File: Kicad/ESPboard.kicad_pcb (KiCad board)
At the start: 2 copper layers, 50.5 x 47.2 mm, 36 parts, among them J1 Controls, J2 GPIO 3.3V, J3 GPIO 5V, J4 Input Power, Q1 BSS138, Q2 BSS138, Q3 BSS138, Q4 BSS138, SW1 Reset, SW2 SW_SPST, SW3 SW_SPST, SW4 SW_SPST, SW5 SW_SPST, U1 ESP8266-01_ESP-01, U2 AMS1117-5.0, U3 AMS1117-3.3

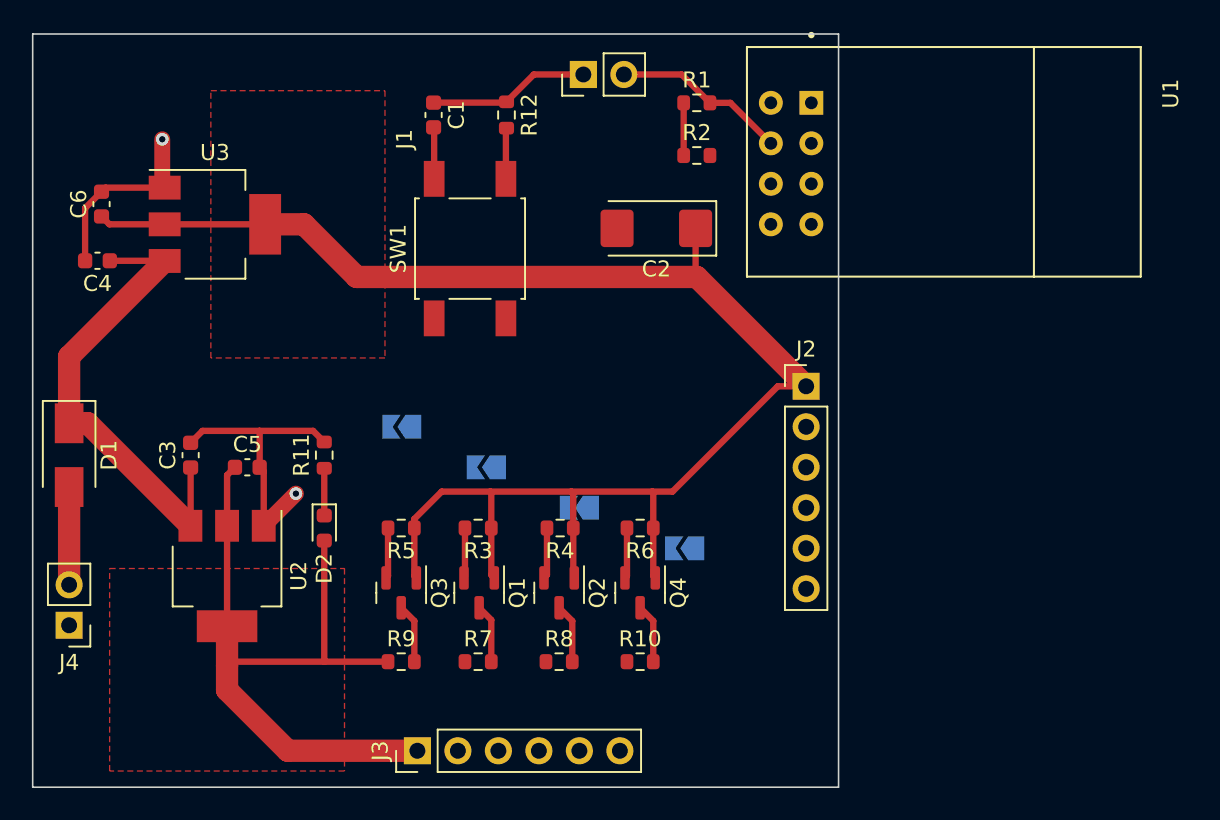
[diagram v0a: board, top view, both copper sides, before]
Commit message: Resized board
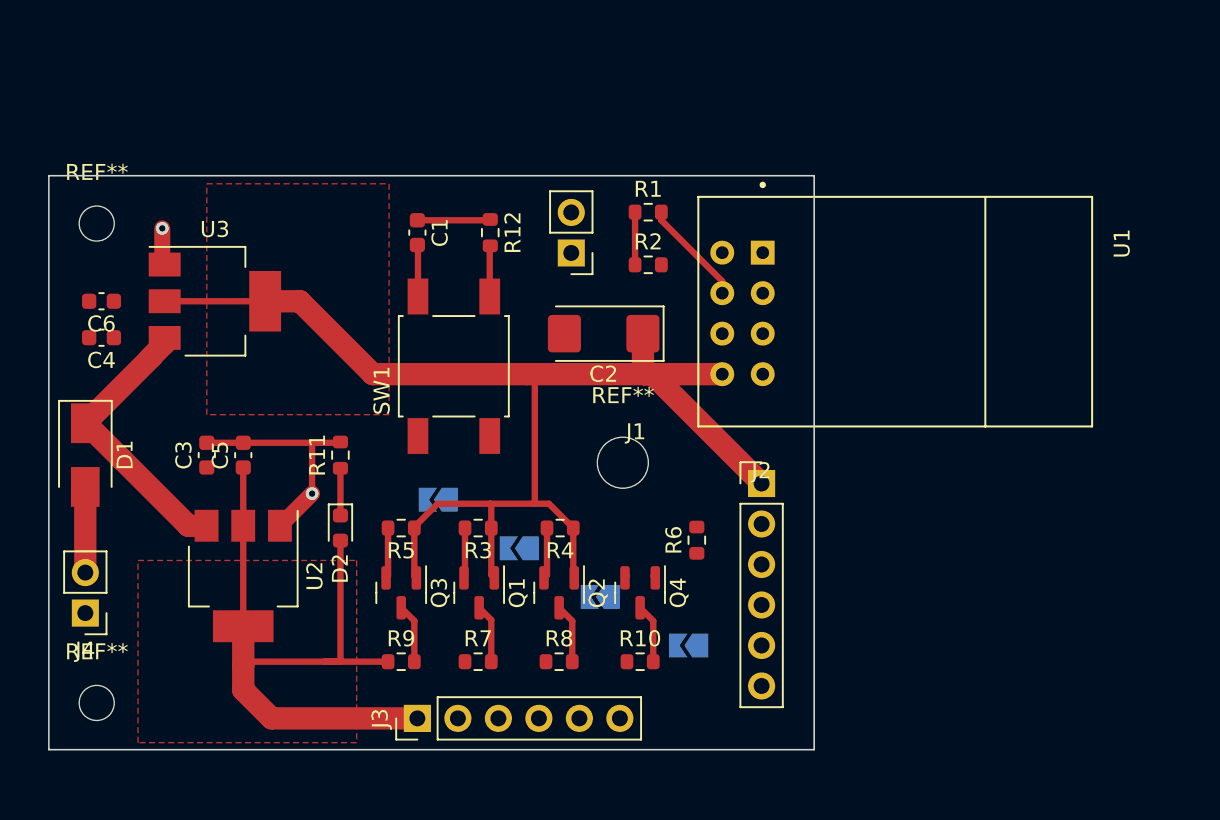
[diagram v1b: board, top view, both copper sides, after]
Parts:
- added REF**: MountingHole_3.2mm_M3, MountingHole:MountingHole_3.2mm_M3, F.Cu at (178.2, 115.5)
- added REF**: MountingHole_2.2mm_M2, MountingHole:MountingHole_2.2mm_M2, F.Cu at (145.2, 100.5)
- added REF**: MountingHole_2.2mm_M2, MountingHole:MountingHole_2.2mm_M2, F.Cu at (145.2, 130.6)
- moved J1 11.2 mm to (175.0, 102.4), turned to 180 degrees
- moved U1 9.88 mm to (195.3, 106.2)
- moved R1 7.50 mm to (179.8, 99.8)
- moved R2 7.50 mm to (179.8, 103.1)
- moved R12 7.45 mm to (169.9, 101.1)
- moved C1 7.45 mm to (165.4, 101.1)
- moved SW1 7.45 mm to (167.6, 109.5)
- moved C2 7.38 mm to (177.0, 107.4)
- moved J2 6.71 mm to (186.9, 116.8)
- moved SW5 6.10 mm to (182.4, 127.0)
- moved C6 6.10 mm to (145.5, 105.4), turned to 180 degrees
- moved SW3 5.74 mm to (176.8, 124.0)
- moved SW2 5.49 mm to (171.7, 120.9)
- moved SW4 5.11 mm to (166.7, 117.9)
- moved C4 4.83 mm to (145.5, 107.7)
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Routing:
- net +3.3V: track 103.3 -> 83.8 mm
- net GND: track 33.1 -> 20.0 mm
- net VCC: track 30.0 -> 17.9 mm
- net Net-(C1-Pad1): track 10.1 -> 4.59 mm
- net Net-(J1-Pad2): track 11.0 -> 6.66 mm
- net Net-(Q4-Pad2): track 3.18 -> 0.18 mm
- net +5V: track 45.5 -> 43.4 mm
- net Net-(D1-Pad2): track 6.13 -> 5.37 mm
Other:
- board size 50.5 x 47.2 mm -> 48 x 36 mm

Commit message: Routing complete
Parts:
- renumbered REF** to H1, REF** to H2, REF** to H3
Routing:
- net Net-(J2-Pad4): track 0.00 -> 35.8 mm
- net Net-(J2-Pad3): track 0.00 -> 33.1 mm
- net Net-(J2-Pad2): track 0.00 -> 31.7 mm
- net Net-(J2-Pad5): track 0.00 -> 24.6 mm
- net Net-(C1-Pad1): track 4.59 -> 28.0 mm
- net GND: track 20.0 -> 43.2 mm, vias 2 -> 3
- net +3.3V: track 83.8 -> 102.0 mm
- net +5V: track 43.4 -> 61.1 mm, vias 0 -> 2
- net Net-(Q4-Pad2): track 0.18 -> 16.1 mm, vias 0 -> 1
- net Net-(J3-Pad4): track 3.72 -> 11.5 mm
- net Net-(J1-Pad2): track 6.66 -> 13.8 mm
- net VCC: track 17.9 -> 24.7 mm
- net Net-(Q2-Pad2): track 3.20 -> 9.68 mm, vias 0 -> 1
- net Net-(Q1-Pad2): track 3.15 -> 9.28 mm, vias 0 -> 1
- net Net-(J3-Pad5): track 3.72 -> 9.83 mm
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- added copper zone on B.Cu, net GND

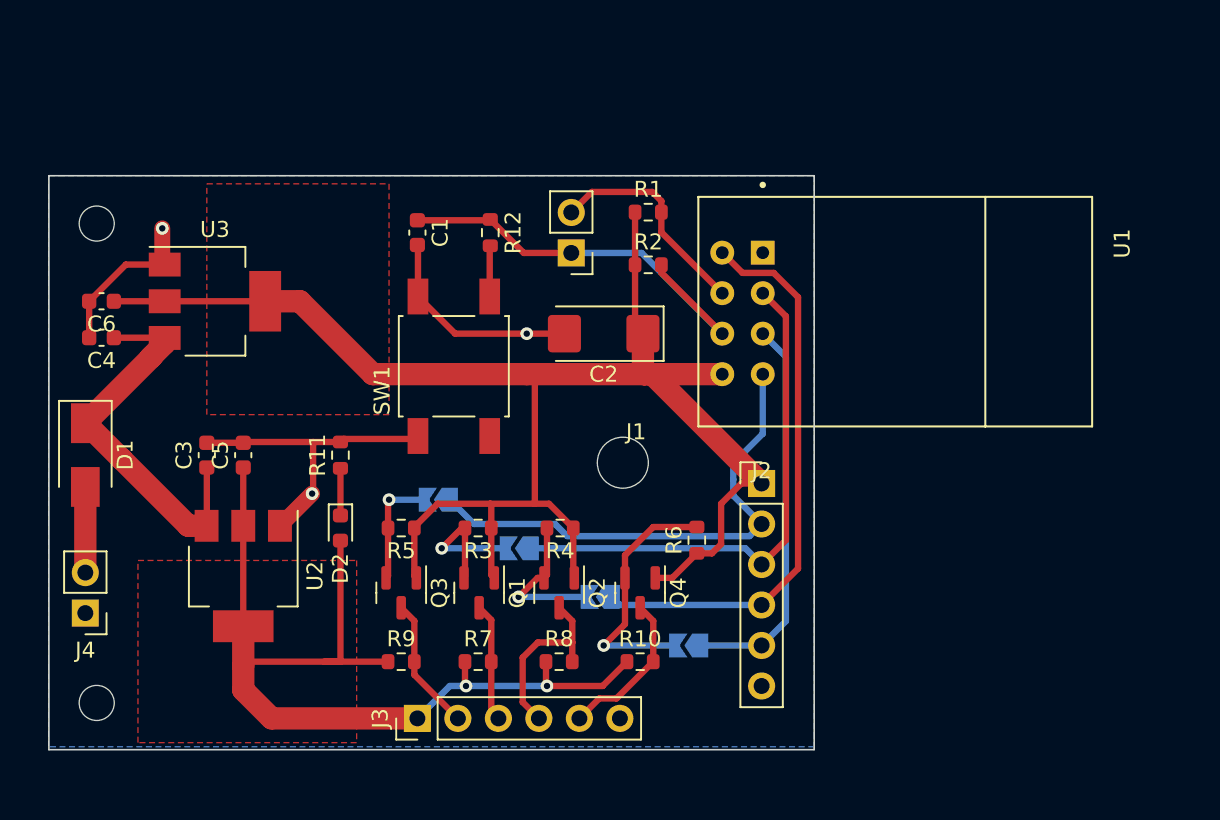
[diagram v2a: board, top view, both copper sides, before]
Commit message: Added silkscreen
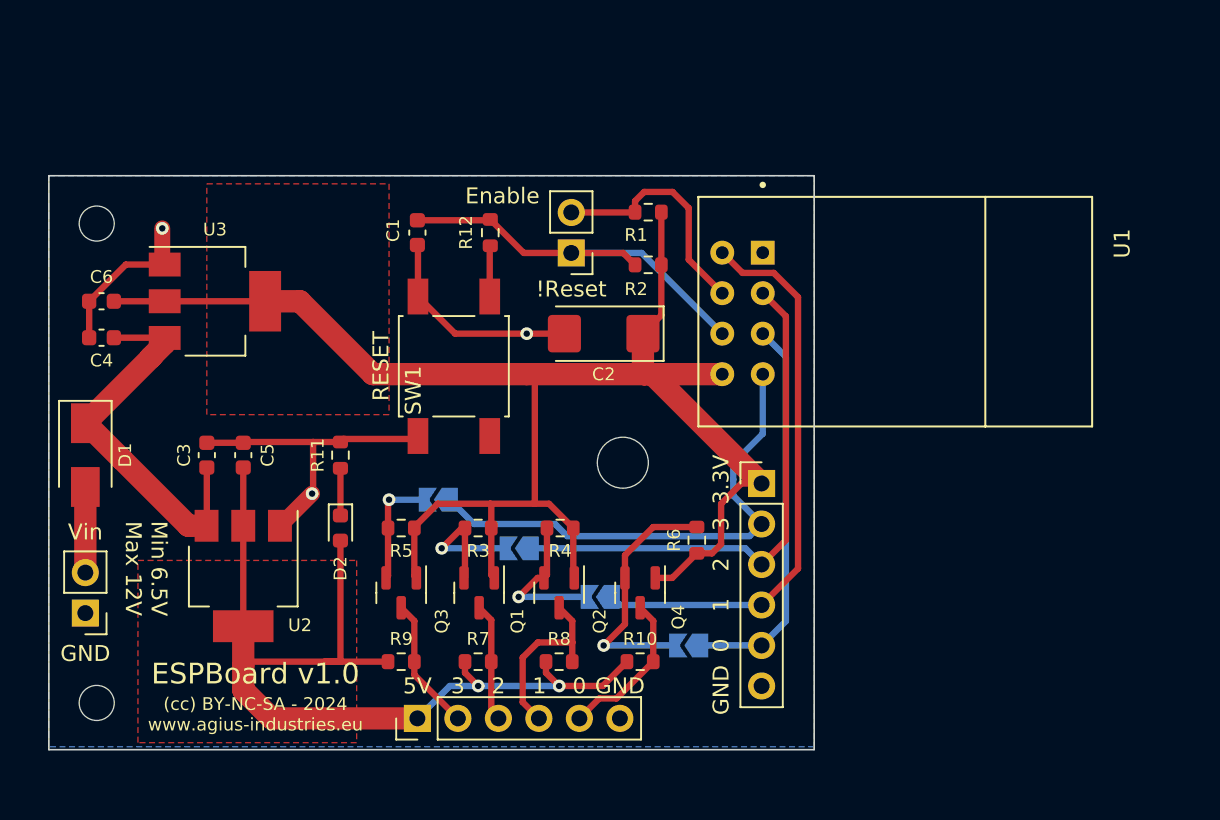
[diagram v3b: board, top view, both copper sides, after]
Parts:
- turned R1 to 180 degrees
- turned R2 to 180 degrees
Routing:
- net Net-(C1-Pad1): track 28.0 -> 26.4 mm
- net Net-(J1-Pad2): track 13.8 -> 14.9 mm
- net +3.3V: track 102.0 -> 102.9 mm
- net +5V: track 61.1 -> 61.8 mm
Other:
- board text added: "!Reset"
- board text added: "(cc) BY-NC-SA - 2024 www.agius-industries.eu"
- board text added: "0"
- board text added: "1"
- board text added: "2"
- board text added: "3"
- board text added: "3.3V"
- board text added: "5V"
- board text added: "ESPBoard v1.0"
- board text added: "Enable"
- board text added: "GND"
- board text added: "GPIO 0"
- board text added: "GPIO 1.Tx"
- board text added: "GPIO 2"
- board text added: "GPIO 3.Rx"
- board text added: "GPIO 5V Level shifter"
- board text added: "M2"
- board text added: "M3"
- board text added: "Min 6.5V Max 12V"
- board text added: "RESET"
- board text added: "Vin"

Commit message: Minor adjustments
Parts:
- added G1: LOGO, LOGO, B.Cu at (150.4, 121.7)
- C2: value 220µF -> 220uF
- C3, C4, C5, C6: value 22µF -> 22uF
- moved J2 12.7 mm to (186.9, 129.5), turned to 180 degrees
- moved J3 12.7 mm to (178.1, 131.6), turned to -90 degrees
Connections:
- J2 pad 1: +3.3V -> GND
- J2 pad 6: GND -> +3.3V
- J3 pad 1: +5V -> GND
- J3 pad 6: GND -> +5V
- Q1 pad 3: Net-(J3-Pad3) -> Net-(J3-Pad4)
- Q2 pad 3: Net-(J3-Pad4) -> Net-(J3-Pad3)
- Q3 pad 3: Net-(J3-Pad2) -> Net-(J3-Pad5)
- Q4 pad 3: Net-(J3-Pad5) -> Net-(J3-Pad2)
- R10 pad 2: Net-(J3-Pad5) -> Net-(J3-Pad2)
- R7 pad 2: Net-(J3-Pad3) -> Net-(J3-Pad4)
- R8 pad 2: Net-(J3-Pad4) -> Net-(J3-Pad3)
- R9 pad 2: Net-(J3-Pad2) -> Net-(J3-Pad5)
- SW2 pad 1: Net-(J2-Pad3) -> Net-(J2-Pad4)
- SW3 pad 1: Net-(J2-Pad4) -> Net-(J2-Pad3)
- SW4 pad 1: Net-(J2-Pad2) -> Net-(J2-Pad5)
- SW5 pad 1: Net-(J2-Pad5) -> Net-(J2-Pad2)
- U1 pad 2: Net-(J2-Pad3) -> Net-(J2-Pad4)
- U1 pad 3: Net-(J2-Pad5) -> Net-(J2-Pad2)
- U1 pad 4: Net-(J2-Pad2) -> Net-(J2-Pad5)
- U1 pad 5: Net-(J2-Pad4) -> Net-(J2-Pad3)
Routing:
- net Net-(J2-Pad5): track 24.6 -> 31.7 mm
- net Net-(J2-Pad2): track 31.7 -> 24.6 mm
- net GND: track 43.2 -> 38.2 mm
- net Net-(J3-Pad4): track 11.5 -> 7.44 mm
- net Net-(J3-Pad3): track 7.44 -> 11.5 mm
- net Net-(J2-Pad4): track 35.8 -> 33.1 mm
- net Net-(J2-Pad3): track 33.1 -> 35.8 mm
- net Net-(J3-Pad5): track 9.83 -> 8.41 mm
- net Net-(J3-Pad2): track 8.41 -> 9.83 mm
- net +3.3V: track 102.9 -> 102.2 mm
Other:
- board text added: "5V Level shifter"
- board text added: "Designed in European Union"
- board text removed: "GPIO 5V Level shifter"

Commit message: Added photos
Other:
- board text added: "TODO: - Increase connector size for screw terminas - Change ESP-01 orientation to cover board"
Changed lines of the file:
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@@
     (effects (font (size 1 1) (thickness 0.15)))
+  )
+  (gr_text "TODO:\n - Increase connector size for screw terminas\n - Change ESP-01 orientation to cover board" (at 165.989 146.431) (layer "Dwgs.User")
+    (effects (font (size 1.5 1.5) (thickness 0.3)))
   )
   (segment (start 178.263 102.38) (end 175.006 102.38) (width 0.4) (layer "F.Cu") (net 1))
